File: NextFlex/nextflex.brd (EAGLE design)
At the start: 160 x 100 mm, 2 parts, among them J1 FFC-32, J2 FFC-32

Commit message: more nextflex progress
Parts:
- added C1, C2, C7, C8: 1uF, scono:0603-CAP
- added C3, C4: 18pF, scono:0603-CAP
- added C5, C6: 2.2uF, scono:0603-CAP
- added D1, D2: (no value), scono:CZRU
- added D4, D7: RED, scono:LED-0603
- added D5: NIR, scono:LED-0603
- added D6: OPD, scono:LED-1206
- added D8: YELLOW, scono:LED-0603
- added D9: GREEN, scono:LED-0603
- added J3: (no value), scono:1X10
- added J4, J5: (no value), scono:1X02
- added J6: (no value), scono:1X06
- added J7: (no value), scono:1X04
- added J8: FFC-32, scono:MOLEX_503480-3200
- added JP1, JP2: JUMPER-SMT_2_NC_TRACE_NO-SILK, scono:SMT-JUMPER_2_NC_TRACE_NO-SILK
- added Q1: (no value), scono:XTAL_ECS-80-18-5PX-TR
- added R1, R2: 10k, scono:0603-RES
- added R3: 330R, scono:EXB2HV
- added R7, R8: 330R, scono:0603-RES
- added R9: 1k, scono:0603-RES
- added R_CAL, R_FB: 100k, scono:0603-RES
- added S1: (no value), scono:DP3T
- added TP3, TP4, VIN, VOUT: TEST_POINTTHRU, scono:TEST_POINT
- added U1, U2: DG406DYZ-T, scono:SOIC127P1032X265-28N
- added U3: AD5933YRSZ, scono:RS_16
- added U4: AFE4490_AFE4490, scono:AFE4490_QFN40-6X6
- added U5: AZ1117EH-3.3TRG1, scono:SOT230P700X180-4N
- added U6: LM340SX-5.0/NOPB, scono:TS3B
- J2: value FFC-32 -> (none); device scono:MOLEX_503480-3200 -> scono:1X02
- moved J2 25.9 mm to (10.5, 22.2)
- moved J1 8.51 mm to (18.5, 3.00)
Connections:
- new net 3.3V: C2.1, C7.1, D7.A, JP2.2, U4.20, U4.29, U4.31, U4.33, U4.39, U5.2, U5.4
- new net 5V: C8.1, J6.6, U4.11, U4.17, U4.18, U5.3
- new net 9V: J8.11, J8.12, J8.27, J8.28
- new net ADC_RDY: U4.28
- new net BG: C5.1, U4.7
- new net E1: J1.1, J1.2, U1.19, U2.19
- new net E10: J1.19, J1.20, U1.10, U2.10
- new net E11: J1.21, J1.22, U1.9, U2.9
- new net E12: J1.23, J1.24, U1.8, U2.8
- new net E13: J1.25, J1.26, U1.7, U2.7
- new net E14: J1.27, J1.28, U1.6, U2.6
- new net E15: J1.29, J1.30, U1.5, U2.5
- new net E2: J1.3, J1.4, U1.20, U2.20
- new net E3: J1.5, J1.6, U1.21, U2.21
- new net E4: J1.7, J1.8, U1.22, U2.22
- new net E5: J1.10, J1.9, U1.23, U2.23
- new net E6: J1.11, J1.12, U1.24, U2.24
- new net E7: J1.13, J1.14, U1.25, U2.25
- new net E8: J1.15, J1.16, U1.26, U2.26
- new net E9: J1.17, J1.18, U1.11, U2.11
- new net GND: C1.1, C2.2, C3.2, C4.2, C5.2, C6.2, C7.2, C8.2, D1.P, D2.P, J5.1, J5.2, J6.1, R3.10, R3.11, R3.12, R3.13, R3.14, R3.15, R3.16, R3.9, U1.12, U1.27, U2.12, U2.27, U3.12, U3.13, U3.14, U4.12, U4.13, U4.16, U4.19, U4.3, U4.32, U4.36, U4.40, U4.8, U4.EXP@1, U4.EXP@10, U4.EXP@11, U4.EXP@12, U4.EXP@13, U4.EXP@14, U4.EXP@15, U4.EXP@16, U4.EXP@2, U4.EXP@3, U4.EXP@4, U4.EXP@5, U4.EXP@6, U4.EXP@7, U4.EXP@8, U4.EXP@9, U4.PWR@1, U4.PWR@2, U5.1, U6.2, U6.4
- new net GRN: D9.A
- new net IN: U6.1
- new net INN: J7.4, J8.19, J8.20, JP1.2, U4.1
- new net INP: D6.C, J7.3, J8.23, J8.24, U4.2
- new net MUX_1_16: R_CAL.1, TP4.1, U1.4
- new net MUX_1_SEL_0: J3.3, U1.17
- new net MUX_1_SEL_1: J3.4, U1.16
- new net MUX_1_SEL_2: J3.5, U1.15
- new net MUX_1_SEL_3: J3.6, U1.14
- new net MUX_2_16: R_CAL.2, TP3.1, U2.4
- new net MUX_2_SEL_0: J3.7, U2.17
- new net MUX_2_SEL_1: J3.8, U2.16
- new net MUX_2_SEL_2: J3.9, U2.15
- new net MUX_2_SEL_3: J3.10, U2.14
- new net N$16: D4.A, D5.A, JP2.1
- new net N$17: D5.C, R7.1
- new net N$18: D4.C, R8.1
- new net N$19: D6.A, R9.1
- new net N$20: JP1.1, R9.2
- new net N$3: R_FB.2, U3.4
- new net N$5: D7.C, R3.1, R3.2
- new net N$6: D8.C, R3.4, R3.5
- new net N$7: D9.C, R3.7, R3.8
- new net OUT: U6.3
- new net SCL: J3.2, R2.1, U3.16
- new net SDA: J3.1, R1.1, U3.15
- new net SPI_MISO: J6.3, U4.25
- new net SPI_MOSI: J6.4, U4.26
- new net SPI_SCLK: J6.2, U4.24
- new net SPI_SEL: J6.5, U4.27
- new net TXN: D1.N, J7.1, J8.15, J8.16, R7.2, U4.14
- new net TXP: D2.N, J7.2, J8.31, J8.32, R8.2, U4.15
- new net TX_REF: C6.1, U4.9
- new net VCC: C1.2, J4.1, J4.2, R1.2, R2.2, U1.1, U1.18, U2.1, U2.18, U3.10, U3.11, U3.9
- new net VIN: J2.1, U2.28, VIN.1
- new net VIN_AD: J2.2, R_FB.1, U3.5
- new net VOUT: U1.28, U3.6, VOUT.1
- new net XIN: C3.1, Q1.1, U4.38
- new net XOUT: C4.1, Q1.2, U4.37
- new net YEL: D8.A
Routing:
- net GND: track 0.00 -> 95.6 mm, vias 0 -> 9
- net 5V: track 0.00 -> 68.3 mm, vias 0 -> 3
- net INN: track 0.00 -> 46.6 mm, vias 0 -> 2
- net INP: track 0.00 -> 42.0 mm, vias 0 -> 3
- net MUX_1_SEL_3: track 0.00 -> 39.4 mm, vias 0 -> 1
- net MUX_2_SEL_0: track 0.00 -> 33.9 mm, vias 0 -> 1
- net MUX_2_SEL_1: track 0.00 -> 33.3 mm, vias 0 -> 1
- net MUX_2_SEL_2: track 0.00 -> 32.8 mm, vias 0 -> 1
- net MUX_1_SEL_2: track 0.00 -> 28.5 mm, vias 0 -> 1
- net MUX_1_SEL_1: track 0.00 -> 27.3 mm, vias 0 -> 1
- net MUX_1_SEL_0: track 0.00 -> 26.0 mm, vias 0 -> 1
- net TXP: track 0.00 -> 25.9 mm, vias 0 -> 3
- net VIN: track 0.00 -> 25.3 mm
- net E8: track 0.00 -> 24.3 mm, vias 0 -> 2
- net MUX_2_SEL_3: track 0.00 -> 23.9 mm
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- added copper zone on layer 1, net 3.3V
- added copper zone on layer 16, net GND
- added copper zone on layer 1, net VCC
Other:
- board text added: "Arias Research Group Electrode Measurement Design: S.Ono"
- board text added: "CLK"
- board text added: "E1"
- board text added: "E15"
- board text added: "G"
- board text added: "GND"
- board text added: "MISO"
- board text added: "MOSI"
- board text added: "MUX 1 3-2-1-0"
- board text added: "MUX 2 3-2-1-0"
- board text added: "NIR"
- board text added: "Oximeter Test Board"
- board text added: "R"
- board text added: "RED"
- board text added: "SCL SDA"
- board text added: "SEL"
- board text added: "Seiya Ono Fa'19 NextFlex Prototype"
- board text added: "VCC"
- board text added: "Y"

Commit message: finish rev a of nextflex
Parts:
- removed D7: RED, scono:LED-0603
- removed D8: YELLOW, scono:LED-0603
- removed D9: GREEN, scono:LED-0603
- removed J8: FFC-32, scono:MOLEX_503480-3200
- removed R3: 330R, scono:EXB2HV
- removed S1: (no value), scono:DP3T
- added S2: DPDT-SWITCH, scono:SW_JS202011SCQN
- J4: value (none) -> BAT
- J5: value (none) -> FFC-32; device scono:1X02 -> scono:MOLEX_503480-3200
- J6: device scono:1X06 -> scono:1X04
- Q1: device scono:XTAL_ECS-80-18-5PX-TR -> scono:XTAL500X320X130N
- U6: value LM340SX-5.0/NOPB -> LM340MPX-5.0230; device scono:TS3B -> scono:SOT230P700X180-4N
- moved U6 63.8 mm to (48.2, 34.2), turned to 90 degrees
- moved J5 48.3 mm to (36.2, 2.75), turned to 0 degrees
- moved J4 45.1 mm to (47.2, 18.2), turned to 0 degrees
- moved R9 37.2 mm to (33.0, 12.5), turned to 180 degrees
- moved R8 36.4 mm to (33.0, 14.5), turned to 180 degrees
- moved J6 34.7 mm to (34.5, 40.2), turned to 0 degrees
- moved JP1 33.5 mm to (28.0, 12.5), turned to 180 degrees
- moved R7 33.3 mm to (33.0, 10.5), turned to 180 degrees
- moved C4 22.9 mm to (41.0, 26.8)
- moved D2 20.9 mm to (30.0, 14.5), turned to 180 degrees
- moved JP2 20.0 mm to (41.2, 12.5)
- moved D1 20.0 mm to (30.0, 10.5), turned to 180 degrees
- moved D4 19.0 mm to (37.5, 14.5), turned to 180 degrees
- moved D6 18.7 mm to (37.5, 12.5), turned to 0 degrees
- moved Q1 18.6 mm to (36.8, 26.8)
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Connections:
- removed net 9V: J8.11, J8.12, J8.27, J8.28
- removed net GRN: D9.A
- removed net IN: U6.1
- removed net N$5: D7.C, R3.1, R3.2
- removed net N$6: D8.C, R3.4, R3.5
- removed net N$7: D9.C, R3.7, R3.8
- removed net OUT: U6.3
- removed net YEL: D8.A
- new net BAT+: J4.2, S2.1
- new net BAT-: J4.1, S2.4
- net 3.3V: no longer D7.A
- net 5V: now also C1.2, R1.2, R2.2, U1.1, U1.18, U2.1, U2.18, U3.10, U3.11, U3.9, U6.3; no longer J6.6
- net E1: now also J1.31, J1.32; no longer J1.1, J1.2
- net E10: now also J1.13, J1.14; no longer J1.19, J1.20
- net E11: now also J1.11, J1.12; no longer J1.21, J1.22
- net E12: now also J1.10, J1.9; no longer J1.23, J1.24
- net E13: now also J1.7, J1.8; no longer J1.25, J1.26
- net E14: now also J1.5, J1.6; no longer J1.27, J1.28
- net E15: now also J1.3, J1.4; no longer J1.29, J1.30
- net E2: now also J1.29, J1.30; no longer J1.3, J1.4
- net E3: now also J1.27, J1.28; no longer J1.5, J1.6
- net E4: now also J1.25, J1.26; no longer J1.7, J1.8
- net E5: now also J1.23, J1.24; no longer J1.10, J1.9
- net E6: now also J1.21, J1.22; no longer J1.11, J1.12
- net E7: now also J1.19, J1.20; no longer J1.13, J1.14
- net E8: now also J1.17, J1.18; no longer J1.15, J1.16
- net E9: now also J1.15, J1.16; no longer J1.17, J1.18
- net GND: now also S2.5; no longer J5.1, J5.2, J6.1, R3.10, R3.11, R3.12, R3.13, R3.14, R3.15, R3.16, R3.9
- net INN: now also J5.10, J5.9, J7.3; no longer J7.4, J8.19, J8.20
- net INP: now also J5.13, J5.14, J7.2; no longer J7.3, J8.23, J8.24
- net SPI_MOSI: now also J6.2; no longer J6.4
- net SPI_SCLK: now also J6.4; no longer J6.2
- net SPI_SEL: now also J6.1; no longer J6.5
- net TXN: now also J5.5, J5.6, J7.4; no longer J7.1, J8.15, J8.16
- net TXP: now also J5.21, J5.22, J7.1; no longer J7.2, J8.31, J8.32
- net VCC: now also J5.1, J5.17, J5.18, J5.2, S2.2, U6.1; no longer C1.2, J4.1, J4.2, R1.2, R2.2, U1.1, U1.18, U2.1, U2.18, U3.10, U3.11, U3.9
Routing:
- net 5V: track 68.3 -> 12.9 mm
- net 3.3V: track 0.00 -> 49.3 mm, vias 0 -> 2
- net VCC: track 19.3 -> 59.0 mm, vias 2 -> 0
- net INN: track 46.6 -> 27.1 mm, vias 2 -> 3
- net SPI_MISO: track 7.75 -> 23.8 mm, vias 0 -> 1
- net SPI_SCLK: track 8.62 -> 24.5 mm, vias 0 -> 1
- net SPI_MOSI: track 8.10 -> 23.6 mm, vias 0 -> 1
- net SPI_SEL: track 8.94 -> 23.4 mm, vias 0 -> 1
- net TX_REF: track 11.4 -> 1.69 mm, vias 2 -> 0
- net BG: track 11.2 -> 1.48 mm, vias 2 -> 0
- net XIN: track 16.3 -> 8.17 mm
- net XOUT: track 15.7 -> 7.92 mm
- net N$16: track 0.00 -> 7.61 mm
- net GND: track 95.6 -> 101.7 mm, vias 9 -> 11
- net BAT-: track 0.00 -> 4.62 mm
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- added copper zone on layer 1, net 5V
- removed copper zone on layer 1, net 3.3V
- removed copper zone on layer 1, net VCC
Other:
- board size 160 x 100 mm -> 54.5 x 42 mm
- board text added: "Arias Research Group"
- board text added: "NextFlex Rev A S. Ono"
- board text added: "SCK"
- board text added: "SPI"
- board text removed: "Arias Research Group Electrode Measurement Design: S.Ono"
- board text removed: "CLK"
- board text removed: "G"
- board text removed: "GND"
- board text removed: "Oximeter Test Board"
- board text removed: "R"
- board text removed: "Seiya Ono Fa'19 NextFlex Prototype"
- board text removed: "VCC"
- board text removed: "Y"

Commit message: Add bom and clp files for jcl
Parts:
- added U7: TXB0104PWR, scono:PW14
- moved U6 3.13 mm to (49.8, 37.0)
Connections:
- new net SPI_MISO_5V: J6.3, U7.11
- new net SPI_MOSI_5V: J6.2, U7.12
- new net SPI_SCLK_5V: J6.4, U7.10
- new net SPI_SEL_5V: J6.1, U7.13
- net 3.3V: now also U7.1, U7.8
- net 5V: now also U7.14
- net GND: now also U7.7
- net SPI_MISO: now also U7.4; no longer J6.3
- net SPI_MOSI: now also U7.3; no longer J6.2
- net SPI_SCLK: now also U7.5; no longer J6.4
- net SPI_SEL: now also U7.2; no longer J6.1
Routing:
- net 3.3V: track 49.3 -> 64.5 mm, vias 2 -> 3
- net SPI_SEL: track 23.4 -> 9.75 mm, vias 1 -> 2
- net SPI_MOSI: track 23.6 -> 10.5 mm, vias 1 -> 2
- net SPI_MISO: track 23.8 -> 11.6 mm, vias 1 -> 2
- net SPI_SEL_5V: track 0.00 -> 12.0 mm
- net SPI_MOSI_5V: track 0.00 -> 8.69 mm
- net SPI_SCLK: track 24.5 -> 16.3 mm, vias 1 -> 2
- net 5V: track 12.9 -> 20.8 mm, vias 3 -> 5
- net SPI_MISO_5V: track 0.00 -> 6.91 mm
- net SPI_SCLK_5V: track 0.00 -> 6.13 mm
- net GND: track 101.7 -> 104.1 mm, vias 11 -> 13
- net VCC: track 59.0 -> 61.1 mm
- net INP: track 40.7 -> 42.1 mm

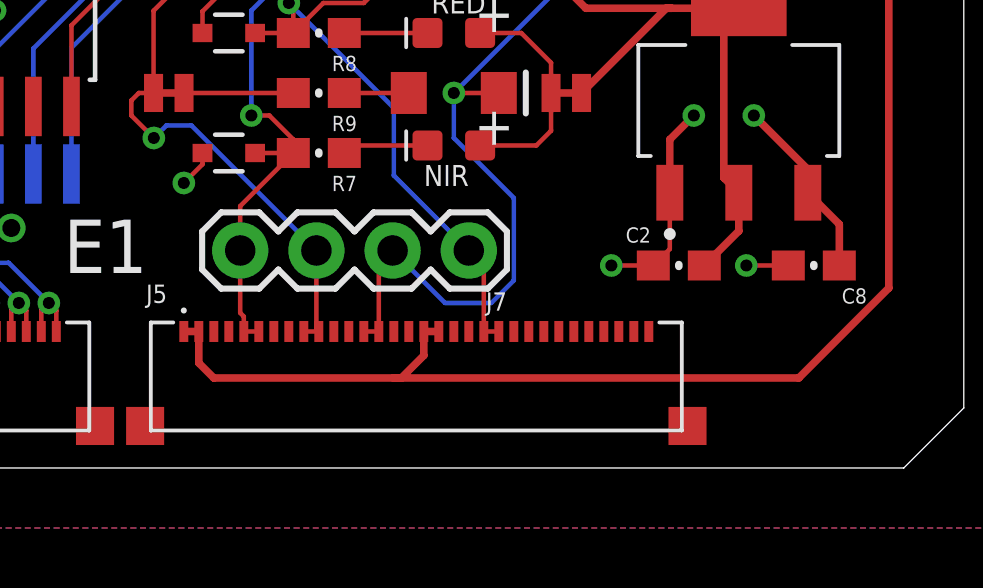
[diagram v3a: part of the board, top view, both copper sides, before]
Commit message: small fixes for anode cathone config
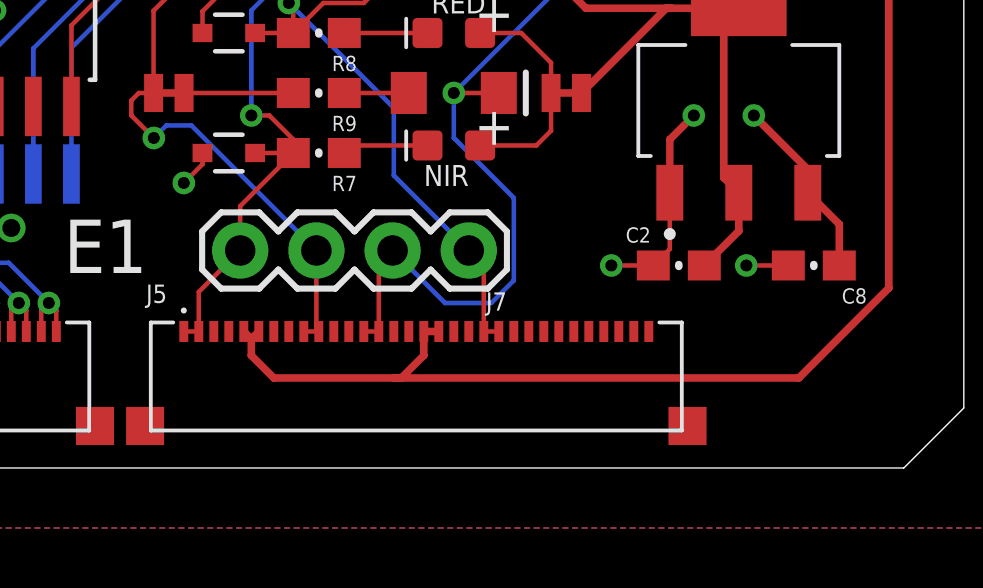
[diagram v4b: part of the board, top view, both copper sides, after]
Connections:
- net TXN: now also J5.1, J5.2; no longer J5.5, J5.6
- net VCC: now also J5.5, J5.6; no longer J5.1, J5.2
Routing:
- net VCC: track 61.1 -> 59.2 mm
- net TXN: track 21.5 -> 22.0 mm
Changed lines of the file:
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@@
 <?xml version="1.0" encoding="utf-8"?>
 <!DOCTYPE eagle SYSTEM "eagle.dtd">
-<eagle version="9.5.1">
+<eagle version="9.5.2">
 <drawing>
 <settings>
@@
 <contactref element="D1" pad="N"/>
 <contactref element="R7" pad="2"/>
-<contactref element="J5" pad="5"/>
-<contactref element="J5" pad="6"/>
 <contactref element="J7" pad="4"/>
 <wire x1="30.8763" y1="10.5" x2="32.15" y2="10.5" width="0.1524" layer="1"/>
@@
 <wire x1="32.15" y1="10.95018125" x2="32.15" y2="10.5" width="0.1524" layer="1"/>
 <wire x1="34" y1="16.25" x2="31.75" y2="16.25" width="0.1524" layer="16"/>
-<wire x1="30.38" y1="7.25" x2="30.38" y2="5.17" width="0.1524" layer="1"/>
-<wire x1="30.5" y1="4.55" x2="31" y2="4.55" width="0.1524" layer="1"/>
 <wire x1="30.75" y1="15.25" x2="30.75" y2="11.75" width="0.1524" layer="16"/>
 <via x="30.75" y="11.75" extent="1-16" drill="0.4"/>
@@
 <wire x1="31.35018125" y1="11.75" x2="32.15" y2="10.95018125" width="0.1524" layer="1"/>
 <wire x1="31.75" y1="16.25" x2="30.75" y2="15.25" width="0.1524" layer="16"/>
-<wire x1="30.5" y1="5.05" x2="30.5" y2="4.55" width="0.1524" layer="1"/>
-<wire x1="30.38" y1="5.17" x2="30.5" y2="5.05" width="0.1524" layer="1"/>
+<contactref element="J5" pad="2"/>
+<contactref element="J5" pad="1"/>
+<wire x1="28.5" y1="4.55" x2="29" y2="4.55" width="0.1524" layer="1"/>
+<wire x1="30.38" y1="7.25" x2="29" y2="5.87" width="0.1524" layer="1"/>
+<wire x1="29" y1="5.87" x2="29" y2="4.55" width="0.1524" layer="1"/>
 </signal>
 <signal name="TXP">
@@
 <wire x1="48" y1="33.375" x2="48" y2="26.75" width="0.508" layer="1"/>
 <wire x1="48" y1="26.75" x2="50" y2="24.75" width="0.508" layer="1"/>
-<contactref element="J5" pad="1"/>
-<contactref element="J5" pad="2"/>
 <contactref element="J5" pad="17"/>
 <contactref element="J5" pad="18"/>
-<wire x1="28.5" y1="4.55" x2="29" y2="4.55" width="0.254" layer="1"/>
-<wire x1="29" y1="4.55" x2="29" y2="3.5" width="0.254" layer="1"/>
-<wire x1="29" y1="3.5" x2="29.5" y2="3" width="0.254" layer="1"/>
 <wire x1="36.5" y1="3.75" x2="36.5" y2="4.55" width="0.254" layer="1"/>
-<wire x1="29.5" y1="3" x2="35.5" y2="3" width="0.254" layer="1"/>
 <wire x1="35.5" y1="3" x2="35.75" y2="3" width="0.254" layer="1"/>
 <wire x1="35.75" y1="3" x2="36.5" y2="3.75" width="0.254" layer="1"/>
 <wire x1="36.5" y1="4.55" x2="37" y2="4.55" width="0.254" layer="1"/>
-<wire x1="35.5" y1="3" x2="49" y2="3" width="0.254" layer="1"/>
+<wire x1="49" y1="3" x2="35.5" y2="3" width="0.254" layer="1"/>
 <wire x1="52" y1="18.5" x2="53.5" y2="20" width="0.254" layer="1"/>
 <wire x1="53.5" y1="20" x2="53.5" y2="23.75" width="0.254" layer="1"/>
@@
 <wire x1="52" y1="6" x2="52" y2="18.5" width="0.254" layer="1"/>
 <wire x1="53.5" y1="23.75" x2="52.5" y2="24.75" width="0.254" layer="1"/>
+<contactref element="J5" pad="5"/>
+<contactref element="J5" pad="6"/>
+<wire x1="35.5" y1="3" x2="31.5" y2="3" width="0.254" layer="1"/>
+<wire x1="31.5" y1="3" x2="30.75" y2="3.75" width="0.254" layer="1"/>
+<wire x1="30.75" y1="3.75" x2="30.75" y2="4.3" width="0.254" layer="1"/>
+<wire x1="30.75" y1="4.3" x2="31" y2="4.55" width="0.254" layer="1"/>
+<wire x1="30.75" y1="4.3" x2="30.5" y2="4.55" width="0.254" layer="1"/>
 </signal>
 <signal name="BAT+" class="1">
